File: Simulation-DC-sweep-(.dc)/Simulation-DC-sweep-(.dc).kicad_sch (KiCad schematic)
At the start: 3 parts

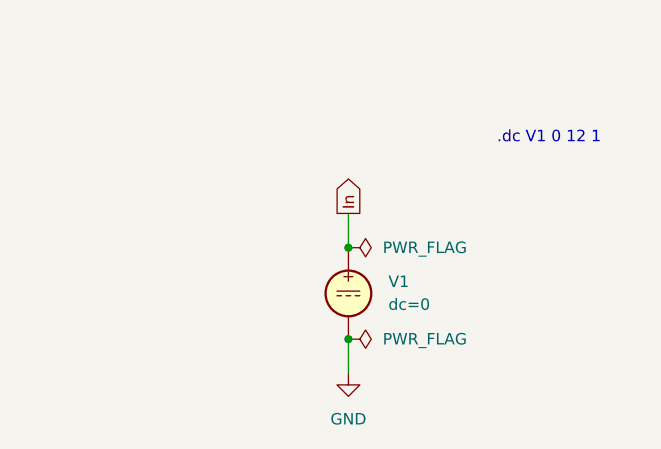
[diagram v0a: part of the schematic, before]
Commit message: Updated all schematics and prepared for KiCad 8.0
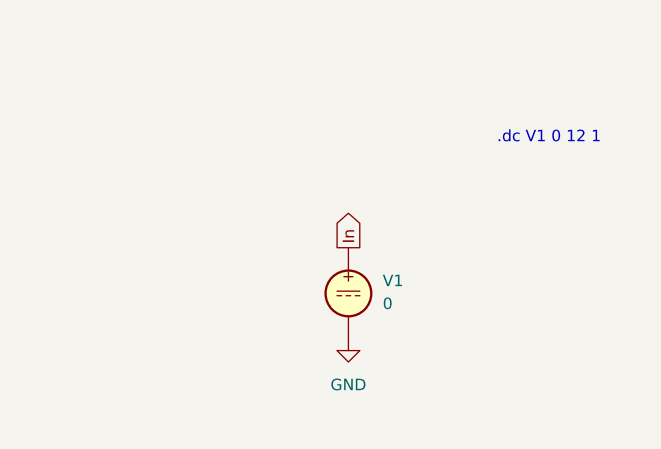
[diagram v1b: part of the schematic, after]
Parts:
- V1: value dc=0 -> 0
